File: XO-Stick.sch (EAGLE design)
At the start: 30 parts, among them J1 POWER, J2 85MOTR, J3 85MOTL, J4 REF, J5 SCL, J6 SDA, J7 AVCC (N/C), J8 AGND (N/C), J9 EXT VCC, SW1 USER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

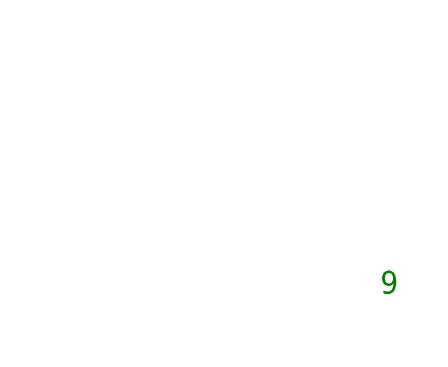
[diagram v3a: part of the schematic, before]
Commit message: XO Stick v10: moved USB connector up 10 mil to better fit vertical XO port.
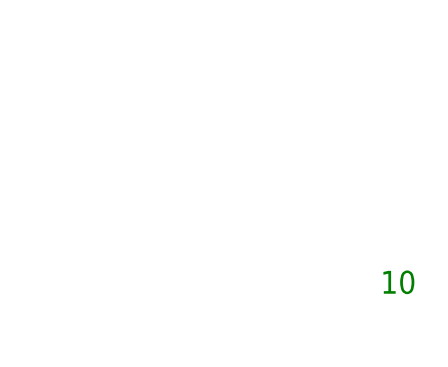
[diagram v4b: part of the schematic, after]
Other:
- note added: "10"
- note removed: "9"
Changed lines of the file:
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@@
 <text x="2.54" y="5.08" size="1.778" layer="97">Altered by SparkFun Electronics (Ryan Owens)</text>
 <text x="149.86" y="27.94" size="5.08" layer="91">XO Stick</text>
-<text x="241.3" y="7.62" size="2.54" layer="91">9</text>
+<text x="241.3" y="7.62" size="2.54" layer="91">10</text>
 <text x="149.86" y="162.56" size="1.778" layer="91"># RIGHT MOTOR 1</text>
 <text x="149.86" y="152.4" size="1.778" layer="91"># SERVO</text>

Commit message: Tweak USB mini-B connector footprint; restring to 8mil min.
USB connector footprint was restricting the min pad width in our restring.
Noticed that USB footprint was really loose, too.  Checked against datasheet,
tightened up holes and switched to oblong pads.  Restring to 8mil min,
which required a few minor trace adjustments.
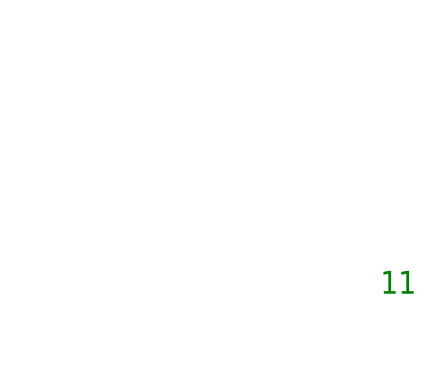
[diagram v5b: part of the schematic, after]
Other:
- note added: "11"
- note removed: "10"
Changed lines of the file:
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@@
 <text x="2.54" y="5.08" size="1.778" layer="97">Altered by SparkFun Electronics (Ryan Owens)</text>
 <text x="149.86" y="27.94" size="5.08" layer="91">XO Stick</text>
-<text x="241.3" y="7.62" size="2.54" layer="91">10</text>
+<text x="241.3" y="7.62" size="2.54" layer="91">11</text>
 <text x="149.86" y="162.56" size="1.778" layer="91"># RIGHT MOTOR 1</text>
 <text x="149.86" y="152.4" size="1.778" layer="91"># SERVO</text>

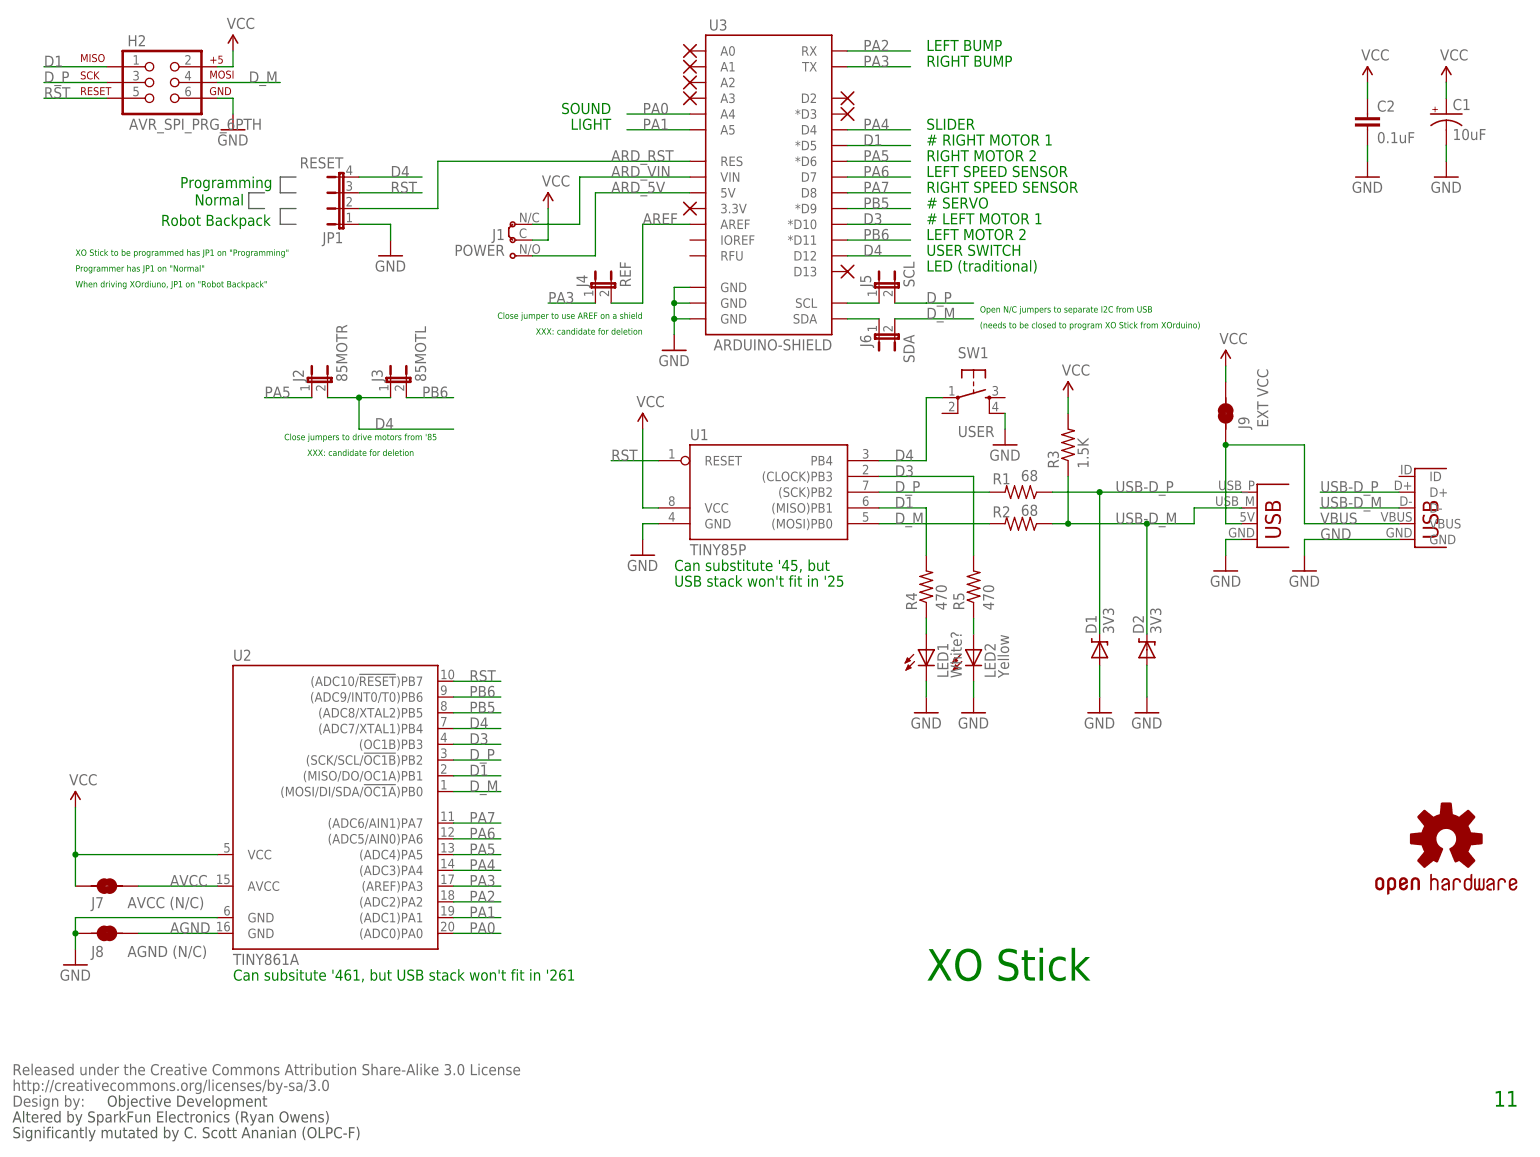
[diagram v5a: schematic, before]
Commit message: Add optional 3.3v TO-92 LDO regulator, for use when unbricking XOs.
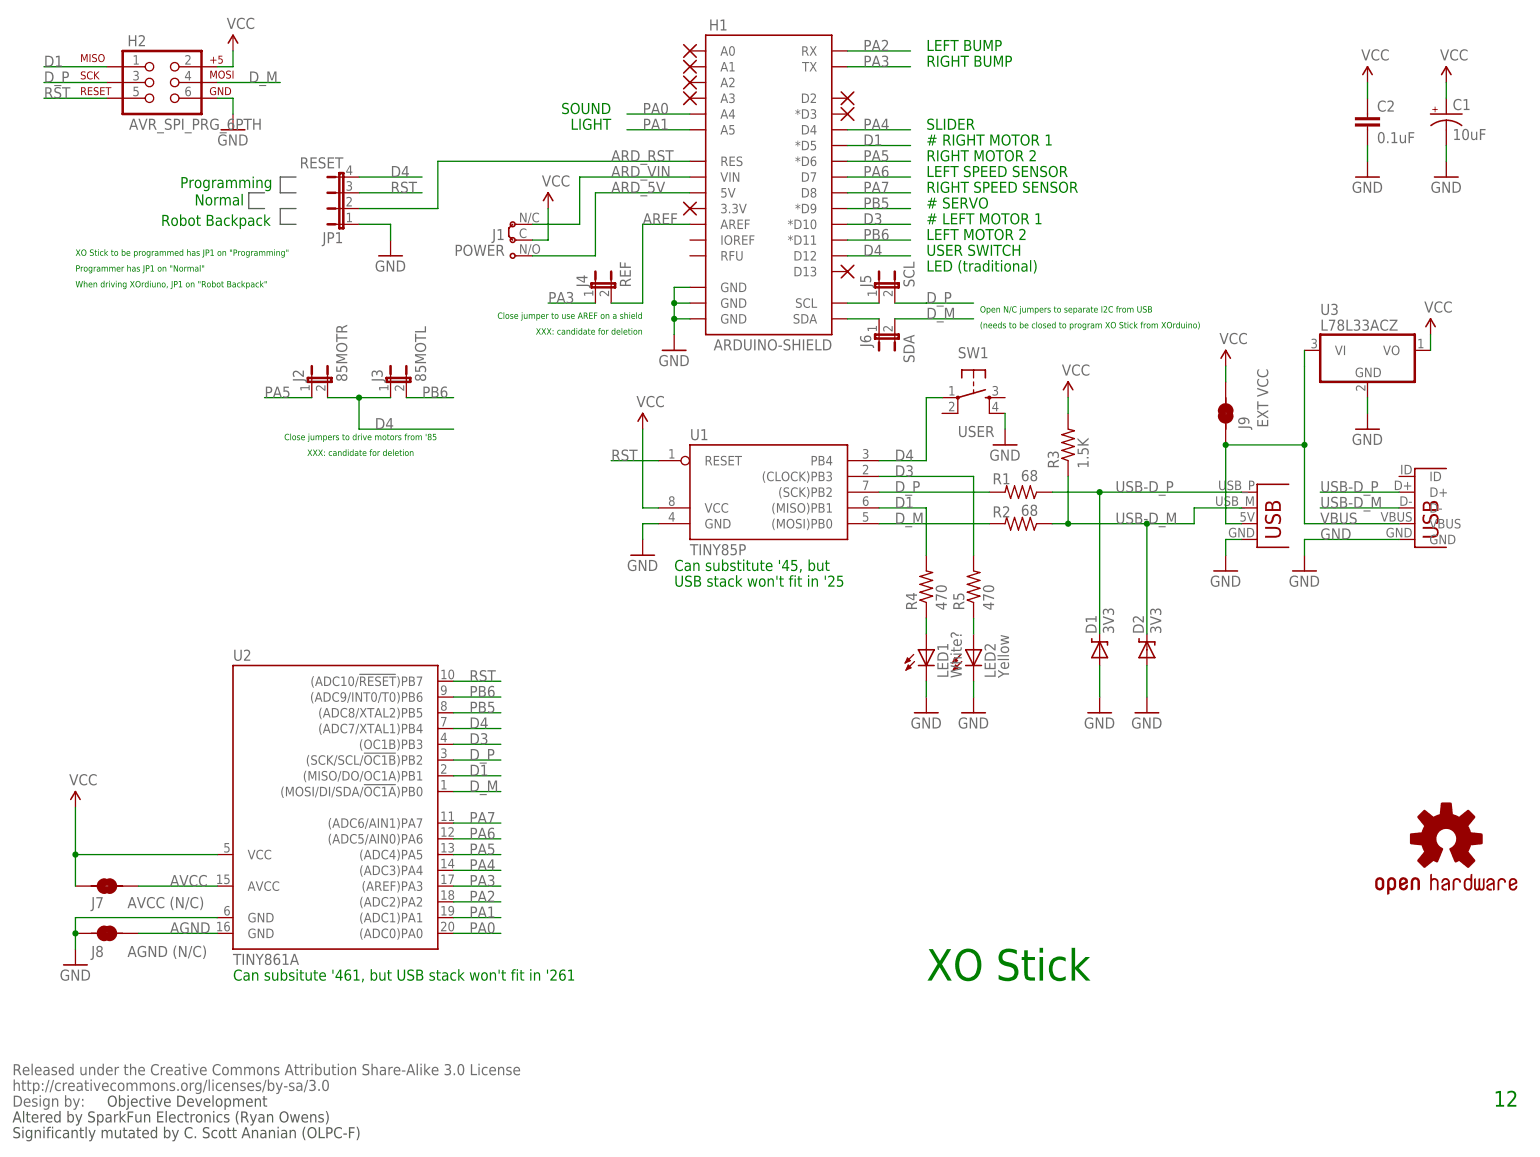
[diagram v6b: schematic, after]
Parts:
- added H1: ARDUINO-SHIELD, xorduino:ARDUINO-SHIELD
- U3: value ARDUINO-SHIELD -> L78L33ACZ; device xorduino:ARDUINO-SHIELD -> linear:78L05Z
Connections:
- net ARD_5V: now also H1.5V; no longer U3.5V
- net ARD_RST: now also H1.RES; no longer U3.RES
- net ARD_VIN: now also H1.VIN; no longer U3.VIN
- net AREF: now also H1.AREF; no longer U3.AREF
- net D1: now also H1.*D5; no longer U3.*D5
- net D3: now also H1.*D10; no longer U3.*D10
- net D4: now also H1.D12; no longer U3.D12
- net GND: now also H1.GND@0, H1.GND@1, H1.GND@2, U3.GND; no longer U3.GND@0, U3.GND@1, U3.GND@2
- net PA0: now also H1.A4; no longer U3.A4
- net PA1: now also H1.A5; no longer U3.A5
- net PA2: now also H1.RX; no longer U3.RX
- net PA3: now also H1.TX; no longer U3.TX
- net PA4: now also H1.D4; no longer U3.D4
- net PA5: now also H1.*D6; no longer U3.*D6
- net PA6: now also H1.D7; no longer U3.D7
- net PA7: now also H1.D8; no longer U3.D8
- net PB5: now also H1.*D9; no longer U3.*D9
- net PB6: now also H1.*D11; no longer U3.*D11
- net SCL: now also H1.SCL; no longer U3.SCL
- net SDA: now also H1.SDA; no longer U3.SDA
- net VBUS: now also U3.VI
- net VCC: now also U3.VO
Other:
- note added: "12"
- note removed: "11"
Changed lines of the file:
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@@
 <part name="GND12" library="SparkFun" deviceset="GND" device=""/>
 <part name="U$1" library="SparkFun" deviceset="OSHW-LOGO" device="M"/>
-<part name="U3" library="xorduino" deviceset="ARDUINO-SHIELD" device=""/>
+<part name="H1" library="xorduino" deviceset="ARDUINO-SHIELD" device=""/>
 <part name="GND13" library="SparkFun" deviceset="GND" device=""/>
 <part name="X3" library="wirepad" deviceset="PAD-N" device=""/>
@@
 <part name="J6" library="xorduino" deviceset="JUMPER-2" device="SJ-NC-BOT" value="SDA"/>
 <part name="J9" library="xorduino" deviceset="SOLDERJUMPER" device="BOT-NOCONFLICT-PAD" value="EXT VCC"/>
+<part name="U3" library="linear" deviceset="78*" device="Z" technology="L05" value="L78L33ACZ"/>
+<part name="P+10" library="SparkFun" deviceset="VCC" device=""/>
+<part name="GND16" library="SparkFun-2" deviceset="GND" device=""/>
 </parts>
 <sheets>
@@
 <text x="2.54" y="5.08" size="1.778" layer="97">Altered by SparkFun Electronics (Ryan Owens)</text>
 <text x="149.86" y="27.94" size="5.08" layer="91">XO Stick</text>
-<text x="241.3" y="7.62" size="2.54" layer="91">11</text>
+<text x="241.3" y="7.62" size="2.54" layer="91">12</text>
 <text x="149.86" y="162.56" size="1.778" layer="91"># RIGHT MOTOR 1</text>
 <text x="149.86" y="152.4" size="1.778" layer="91"># SERVO</text>
@@
 <instance part="GND12" gate="1" x="162.56" y="114.3"/>
 <instance part="U$1" gate="G$1" x="233.68" y="50.8"/>
-<instance part="U3" gate="G$1" x="124.46" y="160.02"/>
+<instance part="H1" gate="G$1" x="124.46" y="160.02"/>
 <instance part="GND13" gate="1" x="109.22" y="129.54"/>
 <instance part="X3" gate="G$1" x="137.16" y="142.24"/>
@@
 <attribute name="VALUE" x="204.978" y="117.094" size="1.778" layer="96" rot="R90"/>
 </instance>
+<instance part="U3" gate="A1" x="220.98" y="129.54"/>
+<instance part="P+10" gate="1" x="231.14" y="132.08"/>
+<instance part="GND16" gate="1" x="220.98" y="116.84"/>
 </instances>
 <busses>
@@
 <wire x1="198.12" y1="127" x2="198.12" y2="124.46" width="0.1524" layer="91"/>
 </segment>
+<segment>
+<pinref part="P+10" gate="1" pin="VCC"/>
+<pinref part="U3" gate="A1" pin="VO"/>
+<wire x1="231.14" y1="132.08" x2="231.14" y2="129.54" width="0.1524" layer="91"/>
+</segment>
 </net>
 <net name="N$7" class="0">
@@
 <segment>
 <pinref part="GND13" gate="1" pin="GND"/>
-<pinref part="U3" gate="G$1" pin="GND@0"/>
+<pinref part="H1" gate="G$1" pin="GND@0"/>
 <wire x1="109.22" y1="132.08" x2="109.22" y2="134.62" width="0.1524" layer="91"/>
 <wire x1="109.22" y1="134.62" x2="111.76" y2="134.62" width="0.1524" layer="91"/>
-<pinref part="U3" gate="G$1" pin="GND@1"/>
+<pinref part="H1" gate="G$1" pin="GND@1"/>
 <wire x1="109.22" y1="134.62" x2="109.22" y2="137.16" width="0.1524" layer="91"/>
 <wire x1="109.22" y1="137.16" x2="111.76" y2="137.16" width="0.1524" layer="91"/>
-<pinref part="U3" gate="G$1" pin="GND@2"/>
+<pinref part="H1" gate="G$1" pin="GND@2"/>
 <wire x1="111.76" y1="139.7" x2="109.22" y2="139.7" width="0.1524" layer="91"/>
 <wire x1="109.22" y1="139.7" x2="109.22" y2="137.16" width="0.1524" layer="91"/>
@@
 <wire x1="58.42" y1="149.86" x2="63.5" y2="149.86" width="0.1524" layer="91"/>
 <wire x1="63.5" y1="149.86" x2="63.5" y2="147.32" width="0.1524" layer="91"/>
+</segment>
+<segment>
+<pinref part="U3" gate="A1" pin="GND"/>
+<pinref part="GND16" gate="1" pin="GND"/>
+<wire x1="220.98" y1="121.92" x2="220.98" y2="119.38" width="0.1524" layer="91"/>
 </segment>
 </net>
@@
 <wire x1="147.32" y1="162.56" x2="137.16" y2="162.56" width="0.1524" layer="91"/>
 <label x="139.7" y="162.56" size="1.778" layer="95"/>
-<pinref part="U3" gate="G$1" pin="*D5"/>
+<pinref part="H1" gate="G$1" pin="*D5"/>
 </segment>
 </net>
@@
 <wire x1="147.32" y1="149.86" x2="137.16" y2="149.86" width="0.1524" layer="91"/>
 <label x="139.7" y="149.86" size="1.778" layer="95"/>
-<pinref part="U3" gate="G$1" pin="*D10"/>
+<pinref part="H1" gate="G$1" pin="*D10"/>
 </segment>
 </net>
@@
 <wire x1="147.32" y1="144.78" x2="137.16" y2="144.78" width="0.1524" layer="91"/>
 <label x="139.7" y="144.78" size="1.778" layer="95"/>
-<pinref part="U3" gate="G$1" pin="D12"/>
+<pinref part="H1" gate="G$1" pin="D12"/>
 </segment>
 <segment>
@@
 <wire x1="101.6" y1="167.64" x2="111.76" y2="167.64" width="0.1524" layer="91"/>
 <label x="104.14" y="167.64" size="1.778" layer="95"/>
-<pinref part="U3" gate="G$1" pin="A4"/>
+<pinref part="H1" gate="G$1" pin="A4"/>
 </segment>
 </net>
@@
 <wire x1="101.6" y1="165.1" x2="111.76" y2="165.1" width="0.1524" layer="91"/>
 <label x="104.14" y="165.1" size="1.778" layer="95"/>
-<pinref part="U3" gate="G$1" pin="A5"/>
+<pinref part="H1" gate="G$1" pin="A5"/>
 </segment>
 </net>
@@
 <segment>
 <label x="139.7" y="177.8" size="1.778" layer="95"/>
-<pinref part="U3" gate="G$1" pin="RX"/>
+<pinref part="H1" gate="G$1" pin="RX"/>
 <wire x1="137.16" y1="177.8" x2="147.32" y2="177.8" width="0.1524" layer="91"/>
 </segment>
@@
 <segment>
 <label x="139.7" y="175.26" size="1.778" layer="95"/>
-<pinref part="U3" gate="G$1" pin="TX"/>
+<pinref part="H1" gate="G$1" pin="TX"/>
 <wire x1="137.16" y1="175.26" x2="147.32" y2="175.26" width="0.1524" layer="91"/>
 </segment>
@@
 <segment>
 <label x="139.7" y="165.1" size="1.778" layer="95"/>
-<pinref part="U3" gate="G$1" pin="D4"/>
+<pinref part="H1" gate="G$1" pin="D4"/>
 <wire x1="137.16" y1="165.1" x2="147.32" y2="165.1" width="0.1524" layer="91"/>
 </segment>
@@
 <segment>
 <label x="139.7" y="160.02" size="1.778" layer="95"/>
-<pinref part="U3" gate="G$1" pin="*D6"/>
+<pinref part="H1" gate="G$1" pin="*D6"/>
 <wire x1="137.16" y1="160.02" x2="147.32" y2="160.02" width="0.1524" layer="91"/>
 </segment>
@@
 <segment>
 <label x="139.7" y="157.48" size="1.778" layer="95"/>
-<pinref part="U3" gate="G$1" pin="D7"/>
+<pinref part="H1" gate="G$1" pin="D7"/>
 <wire x1="137.16" y1="157.48" x2="147.32" y2="157.48" width="0.1524" layer="91"/>
 </segment>
@@
 <segment>
 <label x="139.7" y="154.94" size="1.778" layer="95"/>
-<pinref part="U3" gate="G$1" pin="D8"/>
+<pinref part="H1" gate="G$1" pin="D8"/>
 <wire x1="137.16" y1="154.94" x2="147.32" y2="154.94" width="0.1524" layer="91"/>
 </segment>
@@
 </segment>
 <segment>
-<pinref part="U3" gate="G$1" pin="*D11"/>
+<pinref part="H1" gate="G$1" pin="*D11"/>
 <wire x1="137.16" y1="147.32" x2="147.32" y2="147.32" width="0.1524" layer="91"/>
 <label x="139.7" y="147.32" size="1.778" layer="95"/>
@@
 <wire x1="147.32" y1="152.4" x2="137.16" y2="152.4" width="0.1524" layer="91"/>
 <label x="139.7" y="152.4" size="1.778" layer="95"/>
-<pinref part="U3" gate="G$1" pin="*D9"/>
+<pinref part="H1" gate="G$1" pin="*D9"/>
 </segment>
 </net>
 <net name="ARD_RST" class="0">
 <segment>
-<pinref part="U3" gate="G$1" pin="RES"/>
+<pinref part="H1" gate="G$1" pin="RES"/>
 <wire x1="71.12" y1="160.02" x2="111.76" y2="160.02" width="0.1524" layer="91"/>
 <label x="99.06" y="160.02" size="1.778" layer="95"/>
@@
 <net name="SCL" class="0">
 <segment>
-<pinref part="U3" gate="G$1" pin="SCL"/>
+<pinref part="H1" gate="G$1" pin="SCL"/>
 <wire x1="137.16" y1="137.16" x2="142.24" y2="137.16" width="0.1524" layer="91"/>
 <pinref part="J5" gate="G$1" pin="1"/>
@@
 <net name="SDA" class="0">
 <segment>
-<pinref part="U3" gate="G$1" pin="SDA"/>
+<pinref part="H1" gate="G$1" pin="SDA"/>
 <wire x1="137.16" y1="134.62" x2="142.24" y2="134.62" width="0.1524" layer="91"/>
 <pinref part="J6" gate="G$1" pin="1"/>
@@
 <net name="AREF" class="0">
 <segment>
-<pinref part="U3" gate="G$1" pin="AREF"/>
+<pinref part="H1" gate="G$1" pin="AREF"/>
 <wire x1="104.14" y1="137.16" x2="104.14" y2="149.86" width="0.1524" layer="91"/>
 <wire x1="104.14" y1="149.86" x2="111.76" y2="149.86" width="0.1524" layer="91"/>
@@
 <wire x1="86.36" y1="149.86" x2="93.98" y2="149.86" width="0.1524" layer="91"/>
 <wire x1="93.98" y1="149.86" x2="93.98" y2="157.48" width="0.1524" layer="91"/>
-<pinref part="U3" gate="G$1" pin="VIN"/>
+<pinref part="H1" gate="G$1" pin="VIN"/>
 <wire x1="93.98" y1="157.48" x2="111.76" y2="157.48" width="0.1524" layer="91"/>
 <label x="99.06" y="157.48" size="1.778" layer="95"/>
@@
 <net name="ARD_5V" class="1">
 <segment>
-<pinref part="U3" gate="G$1" pin="5V"/>
+<pinref part="H1" gate="G$1" pin="5V"/>
 <wire x1="111.76" y1="154.94" x2="96.52" y2="154.94" width="0.1524" layer="91"/>
 <wire x1="96.52" y1="154.94" x2="96.52" y2="144.78" width="0.1524" layer="91"/>
@@
 <wire x1="198.12" y1="114.3" x2="210.82" y2="114.3" width="0.1524" layer="91"/>
 <junction x="198.12" y="114.3"/>
-</segment>
-</net>
+<wire x1="210.82" y1="114.3" x2="210.82" y2="127" width="0.1524" layer="91"/>
+<pinref part="U3" gate="A1" pin="VI"/>
+<wire x1="210.82" y1="127" x2="210.82" y2="129.54" width="0.1524" layer="91"/>
+<junction x="210.82" y="114.3"/>
+</segment>
+</net>
